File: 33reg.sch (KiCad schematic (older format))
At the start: 14 parts, among them P1 TST, P2 TST, P3 TST, P4 TST, U1 AAT1110IJS-3.3-T1

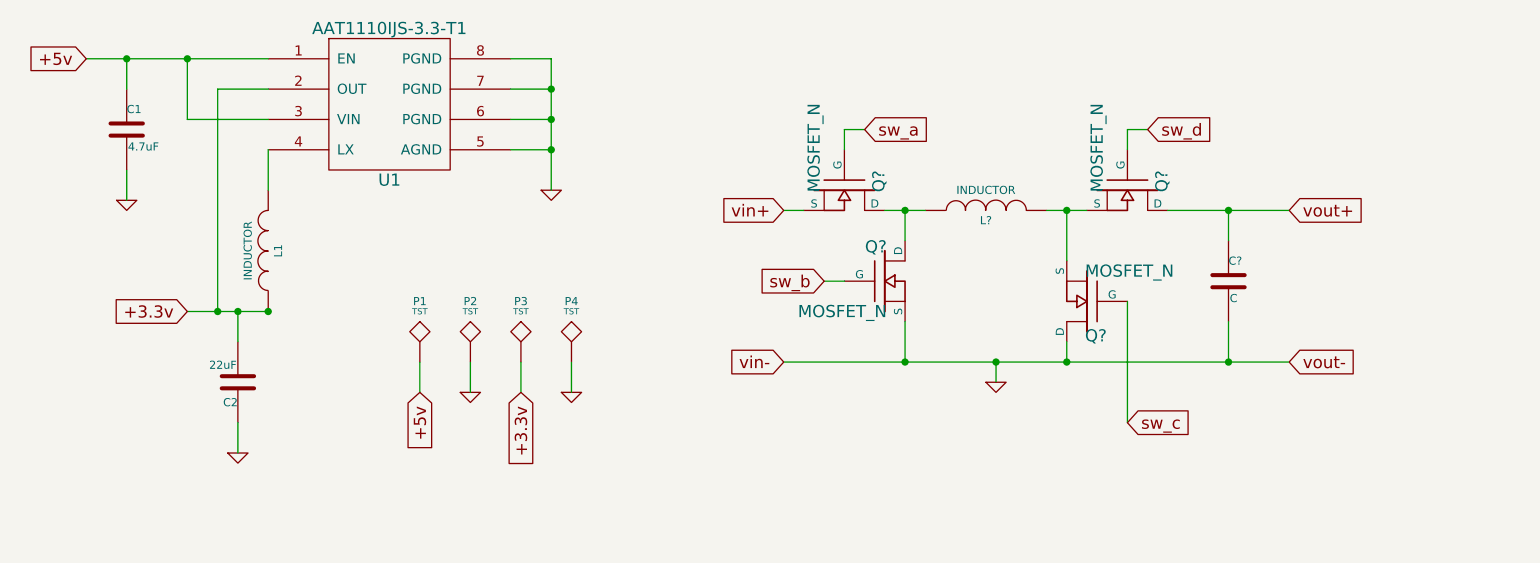
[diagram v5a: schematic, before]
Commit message: - add input cap to 4 switcher
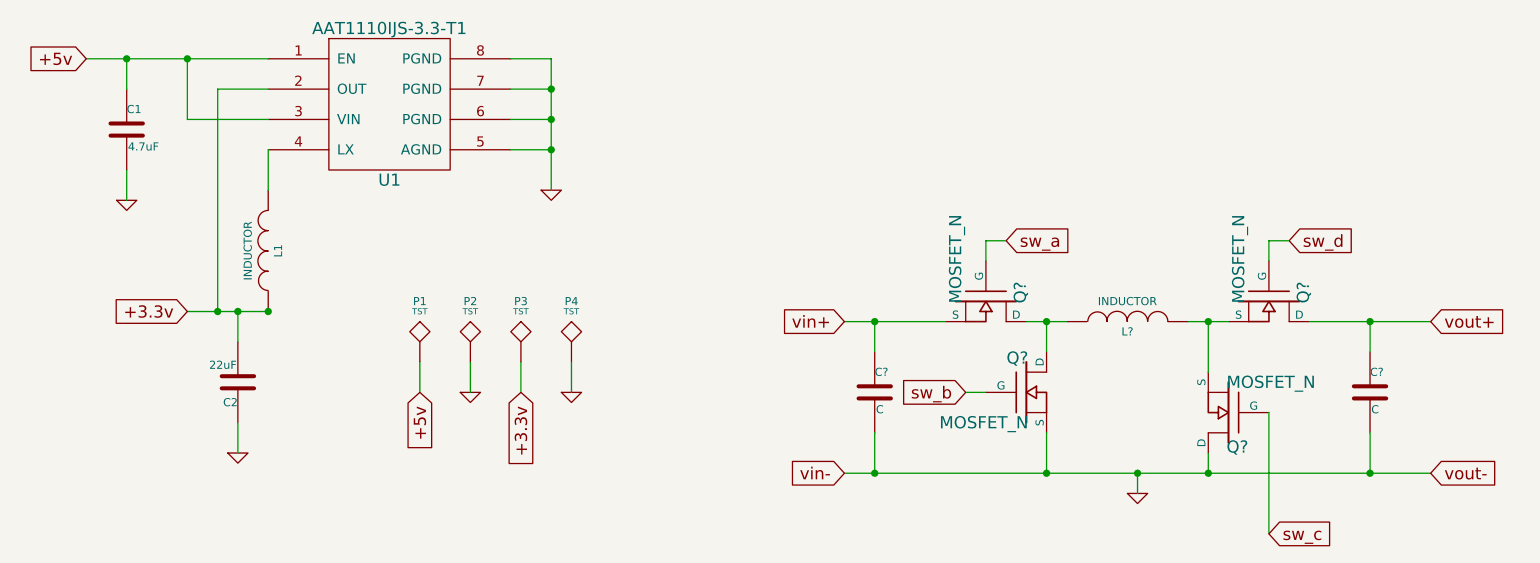
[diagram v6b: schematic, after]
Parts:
- added C?: C, ~, symbol C
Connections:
- net GND: now also C?.2
- net vin+: now also C?.1
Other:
- moved on the sheet: C?, L?, Q?
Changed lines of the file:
@@
 L INDUCTOR L?
 U 1 1 527BCEFC
-P 7850 3950
-F 0 "L?" V 7800 3950 40  0000 C CNN
-F 1 "INDUCTOR" V 7950 3950 40  0000 C CNN
-F 2 "~" H 7850 3950 60  0000 C CNN
-F 3 "~" H 7850 3950 60  0000 C CNN
-	1    7850 3950
+P 8550 4500
+F 0 "L?" V 8500 4500 40  0000 C CNN
+F 1 "INDUCTOR" V 8650 4500 40  0000 C CNN
+F 2 "~" H 8550 4500 60  0000 C CNN
+F 3 "~" H 8550 4500 60  0000 C CNN
+	1    8550 4500
 	0    -1   -1   0
 $EndComp
-Text GLabel 9350 3950 2    60   Input ~ 0
+Text GLabel 10050 4500 2    60   Input ~ 0
 vout+
-Text GLabel 6850 3950 0    60   Input ~ 0
+Text GLabel 7150 4500 0    60   Input ~ 0
 vin+
 $Comp
 L MOSFET_N Q?
 U 1 1 527BCF75
-P 7150 3850
-F 0 "Q?" H 7160 4020 60  0000 R CNN
-F 1 "MOSFET_N" H 7160 3700 60  0000 R CNN
-F 2 "~" H 7150 3850 60  0000 C CNN
-F 3 "~" H 7150 3850 60  0000 C CNN
-	1    7150 3850
+P 7850 4400
+F 0 "Q?" H 7860 4570 60  0000 R CNN
+F 1 "MOSFET_N" H 7860 4250 60  0000 R CNN
+F 2 "~" H 7850 4400 60  0000 C CNN
+F 3 "~" H 7850 4400 60  0000 C CNN
+	1    7850 4400
 	0    1    1    0
 $EndComp
@@
 L MOSFET_N Q?
 U 1 1 527BCF8C
-P 8350 4400
-F 0 "Q?" H 8360 4570 60  0000 R CNN
-F 1 "MOSFET_N" H 8360 4250 60  0000 R CNN
-F 2 "~" H 8350 4400 60  0000 C CNN
-F 3 "~" H 8350 4400 60  0000 C CNN
-	1    8350 4400
+P 9050 4950
+F 0 "Q?" H 9060 5120 60  0000 R CNN
+F 1 "MOSFET_N" H 9060 4800 60  0000 R CNN
+F 2 "~" H 9050 4950 60  0000 C CNN
+F 3 "~" H 9050 4950 60  0000 C CNN
+	1    9050 4950
 	-1   0    0    1
 $EndComp
 Wire Wire Line
-	6850 3950 6950 3950
+	7150 4500 7650 4500
 Wire Wire Line
-	7350 3950 7550 3950
-Connection ~ 7450 3950
+	8050 4500 8250 4500
+Connection ~ 8150 4500
 Wire Wire Line
-	8150 3950 8350 3950
+	8850 4500 9050 4500
 Wire Wire Line
-	8250 3950 8250 4200
-Connection ~ 8250 3950
+	8950 4500 8950 4750
+Connection ~ 8950 4500
 $Comp
 L GND #PWR?
 U 1 1 527BD033
-P 7900 4800
-F 0 "#PWR?" H 7900 4800 30  0001 C CNN
-F 1 "GND" H 7900 4730 30  0001 C CNN
-F 2 "" H 7900 4800 60  0000 C CNN
-F 3 "" H 7900 4800 60  0000 C CNN
-	1    7900 4800
+P 8600 5350
+F 0 "#PWR?" H 8600 5350 30  0001 C CNN
+F 1 "GND" H 8600 5280 30  0001 C CNN
+F 2 "" H 8600 5350 60  0000 C CNN
+F 3 "" H 8600 5350 60  0000 C CNN
+	1    8600 5350
 	1    0    0    -1
 $EndComp
 Wire Wire Line
-	8250 4700 8250 4600
+	8950 5250 8950 5150
 Wire Wire Line
-	6850 4700 9350 4700
-Connection ~ 7900 4700
+	7150 5250 10050 5250
+Connection ~ 8600 5250
 Wire Wire Line
-	7900 4700 7900 4800
+	8600 5250 8600 5350
 Wire Wire Line
-	8750 3950 9350 3950
-Text GLabel 7250 3550 2    60   Input ~ 0
+	9450 4500 10050 4500
+Text GLabel 7950 4100 2    60   Input ~ 0
 sw_a
-Text GLabel 8550 5000 2    60   Input ~ 0
+Text GLabel 9250 5550 2    60   Input ~ 0
 sw_c
 Wire Wire Line
-	7250 3550 7150 3550
+	7950 4100 7850 4100
 Wire Wire Line
-	7150 3550 7150 3650
+	7850 4100 7850 4200
 Wire Wire Line
-	8550 5000 8550 4400
-Text GLabel 6850 4700 0    60   Input ~ 0
+	9250 5550 9250 4950
+Text GLabel 7150 5250 0    60   Input ~ 0
 vin-
-Connection ~ 7450 4700
-Text GLabel 9350 4700 2    60   Input ~ 0
+Connection ~ 8150 5250
+Text GLabel 10050 5250 2    60   Input ~ 0
 vout-
-Connection ~ 8250 4700
+Connection ~ 8950 5250
 $Comp
 L C C?
 U 1 1 527BD302
-P 9050 4300
-F 0 "C?" H 9050 4400 40  0000 L CNN
-F 1 "C" H 9056 4215 40  0000 L CNN
-F 2 "~" H 9088 4150 30  0000 C CNN
-F 3 "~" H 9050 4300 60  0000 C CNN
-	1    9050 4300
+P 9750 4850
+F 0 "C?" H 9750 4950 40  0000 L CNN
+F 1 "C" H 9756 4765 40  0000 L CNN
+F 2 "~" H 9788 4700 30  0000 C CNN
+F 3 "~" H 9750 4850 60  0000 C CNN
+	1    9750 4850
 	1    0    0    -1
 $EndComp
 Wire Wire Line
-	9050 4100 9050 3950
-Connection ~ 9050 3950
+	9750 4650 9750 4500
+Connection ~ 9750 4500
 Wire Wire Line
-	9050 4500 9050 4700
-Connection ~ 9050 4700
+	9750 5050 9750 5250
+Connection ~ 9750 5250
 $Comp
 L MOSFET_N Q?
 U 1 1 527BD436
-P 7350 4300
-F 0 "Q?" H 7360 4470 60  0000 R CNN
-F 1 "MOSFET_N" H 7360 4150 60  0000 R CNN
-F 2 "~" H 7350 4300 60  0000 C CNN
-F 3 "~" H 7350 4300 60  0000 C CNN
-	1    7350 4300
+P 8050 4850
+F 0 "Q?" H 8060 5020 60  0000 R CNN
+F 1 "MOSFET_N" H 8060 4700 60  0000 R CNN
+F 2 "~" H 8050 4850 60  0000 C CNN
+F 3 "~" H 8050 4850 60  0000 C CNN
+	1    8050 4850
 	1    0    0    -1
 $EndComp
 Wire Wire Line
-	7450 4100 7450 3950
+	8150 4650 8150 4500
 Wire Wire Line
-	7450 4500 7450 4700
-Text GLabel 7050 4300 0    60   Input ~ 0
+	8150 5050 8150 5250
+Text GLabel 7750 4850 0    60   Input ~ 0
 sw_b
 Wire Wire Line
-	7050 4300 7150 4300
+	7750 4850 7850 4850
 $Comp
 L MOSFET_N Q?
 U 1 1 527BD4D8
-P 8550 3850
-F 0 "Q?" H 8560 4020 60  0000 R CNN
-F 1 "MOSFET_N" H 8560 3700 60  0000 R CNN
-F 2 "~" H 8550 3850 60  0000 C CNN
-F 3 "~" H 8550 3850 60  0000 C CNN
-	1    8550 3850
+P 9250 4400
+F 0 "Q?" H 9260 4570 60  0000 R CNN
+F 1 "MOSFET_N" H 9260 4250 60  0000 R CNN
+F 2 "~" H 9250 4400 60  0000 C CNN
+F 3 "~" H 9250 4400 60  0000 C CNN
+	1    9250 4400
 	0    1    1    0
 $EndComp
-Text GLabel 8650 3550 2    60   Input ~ 0
+Text GLabel 9350 4100 2    60   Input ~ 0
 sw_d
 Wire Wire Line
-	8650 3550 8550 3550
+	9350 4100 9250 4100
 Wire Wire Line
-	8550 3550 8550 3650
+	9250 4100 9250 4200
+$Comp
+L C C?
+U 1 1 527BD561
+P 7300 4850
+F 0 "C?" H 7300 4950 40  0000 L CNN
+F 1 "C" H 7306 4765 40  0000 L CNN
+F 2 "~" H 7338 4700 30  0000 C CNN
+F 3 "~" H 7300 4850 60  0000 C CNN
+	1    7300 4850
+	1    0    0    -1
+$EndComp
+Wire Wire Line
+	7300 4650 7300 4500
+Connection ~ 7300 4500
+Wire Wire Line
+	7300 5050 7300 5250
+Connection ~ 7300 5250
 $EndSCHEMATC
